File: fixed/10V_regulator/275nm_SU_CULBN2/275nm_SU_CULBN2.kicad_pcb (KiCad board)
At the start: 2 copper layers, 25.4 x 20 mm, 22 parts, among them J1 Conn_01x04, J2 Conn_01x04, M1 MountingHole_2.5mm_Pad, M2 MountingHole_2.5mm_Pad, M3 MountingHole_2.5mm_Pad, M4 MountingHole_2.5mm_Pad, Q1 MMBT5551L, U1 AP3012, U2 LMV321

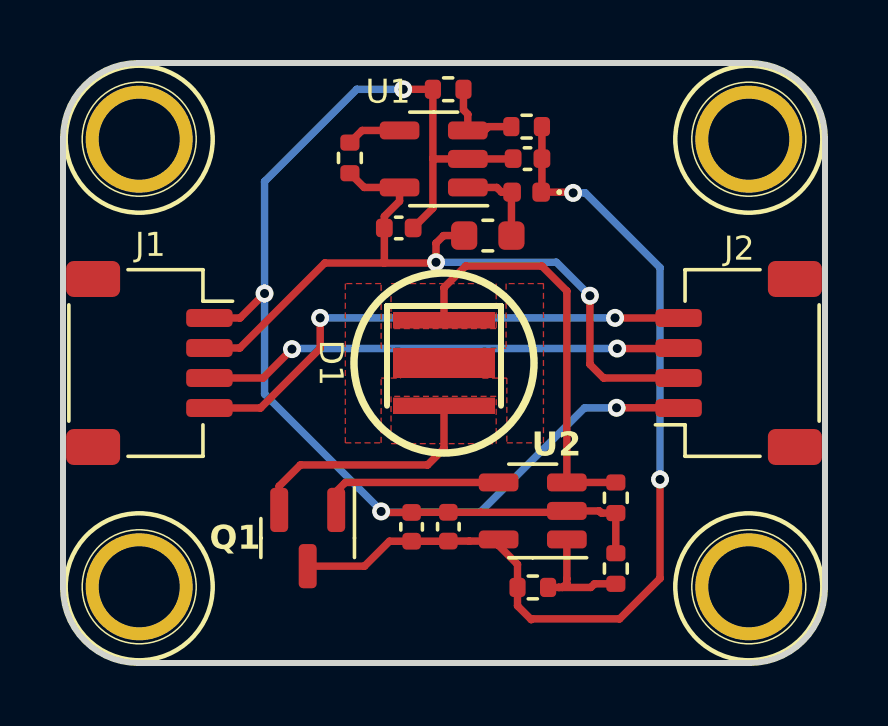
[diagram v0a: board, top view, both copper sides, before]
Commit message: Created initial version of fab files for 275nm LED board.
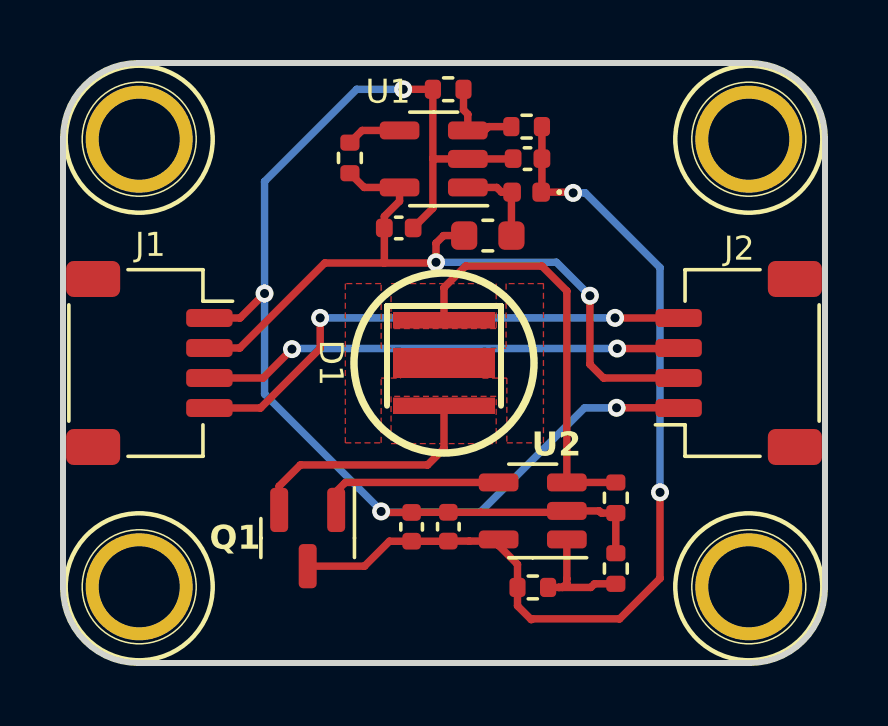
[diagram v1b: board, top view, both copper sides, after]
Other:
- board text added: "IControl HV LED V0.1 R1 www.iorodeo.com 275nm, I=24mA Vin=3.3-5.0V"
- board text removed: "IControl LED V0.1 R2 www.iorodeo.com White, I=24mA Vin=3.3-5.0V"
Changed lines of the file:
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@@
       (drillshape 0)
       (scaleselection 1)
-      (outputdirectory "production/ver_0p1_rev_2/gerber/")
+      (outputdirectory "production/ver_0p1_rev_1/gerber/")
     )
   )
@@
     (descr "Mounting Hole 2.5mm")
     (tags "mounting hole 2.5mm")
-    (attr exclude_from_pos_files exclude_from_bom)
+    (attr board_only exclude_from_pos_files exclude_from_bom)
     (fp_text reference "M1" (at 0 -3.5) (layer "F.SilkS") hide
         (effects (font (size 0.8 0.8) (thickness 0.16)))
@@
     (descr "Mounting Hole 2.5mm")
     (tags "mounting hole 2.5mm")
-    (attr exclude_from_pos_files exclude_from_bom)
+    (attr board_only exclude_from_pos_files exclude_from_bom)
     (fp_text reference "M2" (at 0 -3.5) (layer "F.SilkS") hide
         (effects (font (size 0.8 0.8) (thickness 0.16)))
@@
     (descr "Mounting Hole 2.5mm")
     (tags "mounting hole 2.5mm")
-    (attr exclude_from_pos_files exclude_from_bom)
+    (attr board_only exclude_from_pos_files exclude_from_bom)
     (fp_text reference "M3" (at 0 -3.5) (layer "F.SilkS") hide
         (effects (font (size 0.8 0.8) (thickness 0.16)))
@@
     (descr "Mounting Hole 2.5mm")
     (tags "mounting hole 2.5mm")
-    (attr exclude_from_pos_files exclude_from_bom)
+    (attr board_only exclude_from_pos_files exclude_from_bom)
     (fp_text reference "M4" (at 0 -3.5) (layer "F.SilkS") hide
         (effects (font (size 0.8 0.8) (thickness 0.16)))
@@
   (gr_line (start 75.4 52.5) (end 75.4 67.5)
     (stroke (width 0.2) (type solid)) (layer "Edge.Cuts"))
-  (gr_text "IControl LED V0.1 R2\nwww.iorodeo.com\n\n\n\nWhite, I=24mA\nVin=3.3-5.0V" (at 62.7 60.01) (layer "B.SilkS")
+  (gr_text "IControl HV LED V0.1 R1\nwww.iorodeo.com\n275nm, I=24mA\nVin=3.3-5.0V" (at 62.7 60) (layer "B.SilkS")
     (effects (font (size 1 1) (thickness 0.15)) (justify mirror))
   )
@@
   (segment (start 66.447796 56.642) (end 67.564 57.758204) (width 0.25) (layer "B.Cu") (net 2))
   (segment (start 62.4332 56.642) (end 66.447796 56.642) (width 0.25) (layer "B.Cu") (net 2))
+  (segment (start 69.9008 67.183) (end 68.5546 68.5292) (width 0.25) (layer "F.Cu") (net 3))
   (segment (start 64.5202 65.881) (end 64.5202 66.081) (width 0.25) (layer "F.Cu") (net 3))
   (segment (start 62.8402 65.941) (end 62.8452 65.936) (width 0.25) (layer "F.Cu") (net 3))
   (segment (start 63.5452 65.936) (end 64.4652 65.936) (width 0.25) (layer "F.Cu") (net 3))
-  (segment (start 65.6082 68.5546) (end 65.1502 68.0966) (width 0.25) (layer "F.Cu") (net 3))
   (segment (start 65.9392 54.3052) (end 66.9798 54.3052) (width 0.25) (layer "F.Cu") (net 3))
   (segment (start 65.9638 52.1208) (end 65.9638 53.1876) (width 0.25) (layer "F.Cu") (net 3))
+  (segment (start 65.6082 68.5546) (end 65.1502 68.0966) (width 0.25) (layer "F.Cu") (net 3))
   (segment (start 58.1558 66.772) (end 60.0502 66.772) (width 0.25) (layer "F.Cu") (net 3))
   (segment (start 62.8452 65.936) (end 63.5452 65.936) (width 0.25) (layer "F.Cu") (net 3))
   (segment (start 60.8812 65.941) (end 61.6202 65.941) (width 0.25) (layer "F.Cu") (net 3))
-  (segment (start 68.5546 68.5292) (end 65.6336 68.5292) (width 0.25) (layer "F.Cu") (net 3))
   (segment (start 66.9798 54.3052) (end 67.0052 54.3306) (width 0.25) (layer "F.Cu") (net 3))
   (segment (start 65.1502 66.711) (end 65.1502 67.481) (width 0.25) (layer "F.Cu") (net 3))
   (segment (start 65.9638 53.1876) (end 65.9638 54.2806) (width 0.25) (layer "F.Cu") (net 3))
   (segment (start 64.5202 66.081) (end 65.1502 66.711) (width 0.25) (layer "F.Cu") (net 3))
+  (segment (start 65.1502 68.0966) (end 65.1502 67.481) (width 0.25) (layer "F.Cu") (net 3))
   (segment (start 61.6202 65.941) (end 62.8402 65.941) (width 0.25) (layer "F.Cu") (net 3))
   (segment (start 65.6336 68.5292) (end 65.6082 68.5546) (width 0.25) (layer "F.Cu") (net 3))
-  (segment (start 69.9008 67.183) (end 68.5546 68.5292) (width 0.25) (layer "F.Cu") (net 3))
+  (segment (start 68.5546 68.5292) (end 65.6336 68.5292) (width 0.25) (layer "F.Cu") (net 3))
   (segment (start 65.9638 54.2044) (end 65.9392 54.229) (width 0.25) (layer "F.Cu") (net 3))
-  (segment (start 69.9008 63.881) (end 69.9008 67.183) (width 0.25) (layer "F.Cu") (net 3))
   (segment (start 60.0502 66.772) (end 60.8812 65.941) (width 0.25) (layer "F.Cu") (net 3))
-  (segment (start 65.1502 68.0966) (end 65.1502 67.481) (width 0.25) (layer "F.Cu") (net 3))
+  (segment (start 69.9008 64.3128) (end 69.9008 67.183) (width 0.25) (layer "F.Cu") (net 3))
   (segment (start 64.4652 65.936) (end 64.5202 65.881) (width 0.25) (layer "F.Cu") (net 3))
-  (via (at 69.9008 63.881) (size 0.6) (drill 0.3) (layers "F.Cu" "B.Cu") (net 3))
+  (via (at 69.9008 64.3128) (size 0.6) (drill 0.3) (layers "F.Cu" "B.Cu") (net 3))
   (via (at 67.0052 54.3306) (size 0.6) (drill 0.3) (layers "F.Cu" "B.Cu") (net 3))
-  (segment (start 67.4116 54.3306) (end 69.9008 56.8198) (width 0.25) (layer "B.Cu") (net 3))
-  (segment (start 69.9008 56.8198) (end 69.9008 63.881) (width 0.25) (layer "B.Cu") (net 3))
-  (segment (start 67.0052 54.3306) (end 67.4116 54.3306) (width 0.25) (layer "B.Cu") (net 3))
+  (segment (start 69.9008 56.8198) (end 67.4116 54.3306) (width 0.25) (layer "B.Cu") (net 3))
+  (segment (start 69.9008 64.3128) (end 69.9008 56.8198) (width 0.25) (layer "B.Cu") (net 3))
+  (segment (start 67.4116 54.3306) (end 67.0052 54.3306) (width 0.25) (layer "B.Cu") (net 3))
   (segment (start 70.52 58.5) (end 68.406 58.5) (width 0.25) (layer "F.Cu") (net 4))
   (segment (start 56.5846 61.5) (end 54.98 61.5) (width 0.25) (layer "F.Cu") (net 4))
